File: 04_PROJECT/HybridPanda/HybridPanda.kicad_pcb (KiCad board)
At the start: 4 copper layers, 47.5 x 41.7 mm, 114 parts, among them J1 SWD, P1 TYPE-C-31-M-04, Q1 DDTA143ECA-7-F P08, Q2 DDTA143ECA-7-F P08, Q3 PDTC114EU, Q4 HY12P03C2, SW1 SW_Push, U1 AP22615AWU-7, U10 TJA1042TK-3, U11 TJA1042TK-3, U12 XL1509-3.3, U3 10_0_QHHTZB6_3, U5 FM-B1921RGBA-SH, U6 TPS5450DDAR, U7 STM32H725ZGT6, U8 TJA1042TK-3, U9 TJA1042TK-3, Y1 25MHz X322525MOB4SI

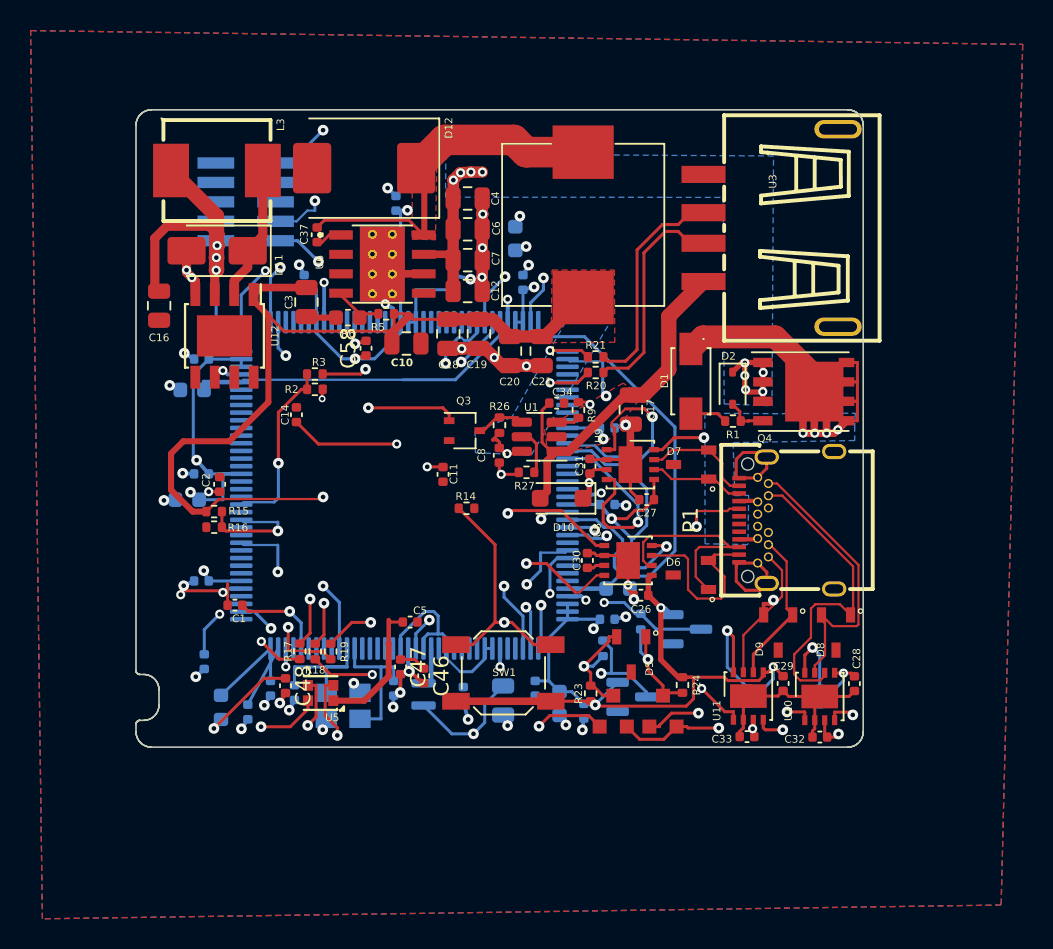
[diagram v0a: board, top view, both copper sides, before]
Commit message: STEP 5: board +5 mm S, U7 +3V3 vias, zone-stub cleanup fix, step5c island/connect_any, D-21..D-24
WIP: pipeline 5a->5b->FR->5c must be rerun from scratch after this commit.

Co-authored-by: Copilot <223556219+Copilot@users.noreply.github.com>
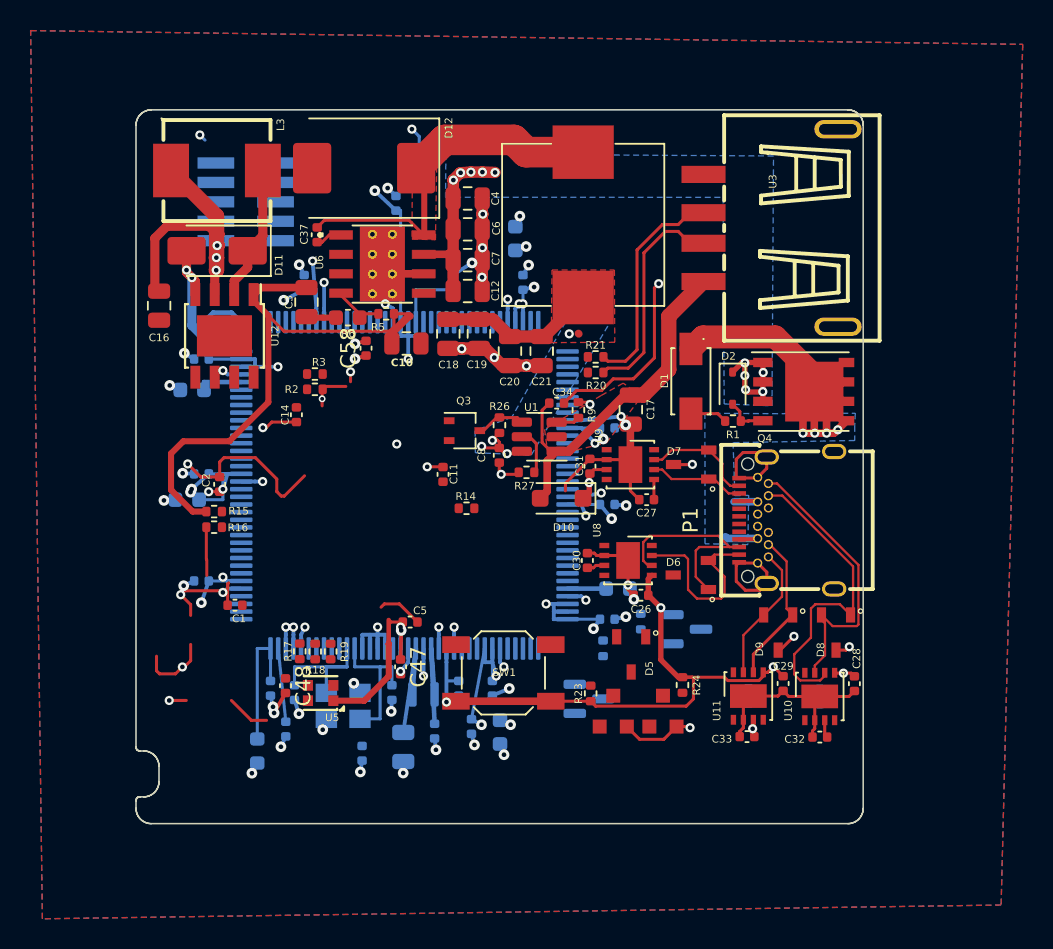
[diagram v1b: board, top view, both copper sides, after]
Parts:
- C46: moved to B.Cu
- moved C38 11.9 mm to (106.7, 74.1)
- moved C63 7.41 mm to (113.9, 72.4)
- moved C42 7.20 mm to (109.4, 73.7)
- moved C60 4.31 mm to (115.8, 72.7)
- moved FB1 3.71 mm to (99.9, 74.0)
- moved C41 3.05 mm to (111.5, 72.7)
- moved D14 2.80 mm to (121.6, 70.6)
- moved C45 2.80 mm to (115.2, 69.9)
- moved C43 2.72 mm to (101.8, 72.5)
- moved C46 2.43 mm to (113.0, 69.9)
- moved C23 0.31 mm to (108.7, 70.1)
- turned L5 to 180 degrees
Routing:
- net GND: track 106.5 -> 181.3 mm, vias 51 -> 66
- net +3V3: track 252.4 -> 187.3 mm, vias 22 -> 40
- net NRST: track 55.1 -> 0.00 mm, vias 3 -> 0
- net VCAP: track 52.0 -> 5.47 mm
- net 12V_Protected: track 61.9 -> 20.1 mm
- net BUS1O_RX: track 38.5 -> 0.00 mm, vias 2 -> 0
- net SBU2_ADC: track 34.4 -> 0.00 mm, vias 2 -> 0
- net BUS1O_TX: track 33.8 -> 0.00 mm, vias 2 -> 0
- net SBU1_ADC: track 33.4 -> 0.00 mm, vias 2 -> 0
- net relay_SBU2: track 33.0 -> 0.00 mm, vias 2 -> 0
- net +5V: track 112.3 -> 82.2 mm, vias 7 -> 8
- net BUS1N_STB: track 29.1 -> 0.00 mm, vias 2 -> 0
- net SBU2: track 27.7 -> 0.00 mm, vias 1 -> 0
- net BUS1N_RX: track 26.2 -> 0.00 mm, vias 2 -> 0
- net LED_BLUE: track 25.5 -> 0.00 mm, vias 2 -> 0
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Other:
- board size 47.5 x 41.7 mm -> 47.5 x 46.7 mm

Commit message: STEP 5-9: PCB routed (DRC 0 unconnected), STEP 6-8 reports, fabrication package (NAO FABRICAR), final report
- STEP 5: pipeline 5a->5b->5c->5d final (run 20), board snapshot .step5_final, DRC 179 (baseline 194), 0 unconnected/clearance/shorts; D-30 extended, D-31 (silk refs)
- STEP 6: step6_reports.py on final board (analytic impedance, skew, vias)
- STEP 7: step7_validate.py - ERC 0 errors, netlist sch x pcb 0 divergences, BOM consistent, parity red_h7 36/36, manifests (ORIGINAL IDENTICAL)
- STEP 8: step8_fabricate.py - gerbers/Excellon/PDF/STEP/BOM_JLC/CPL_JLC + LEIA-ME with blockers
- STEP 9: bring-up plan, RELATORIO_FINAL.md, PROGRESS.md, manifests STEP7/STEP9
- cleanup of tmp probes and pre5c snapshots

Co-authored-by: Copilot <223556219+Copilot@users.noreply.github.com>
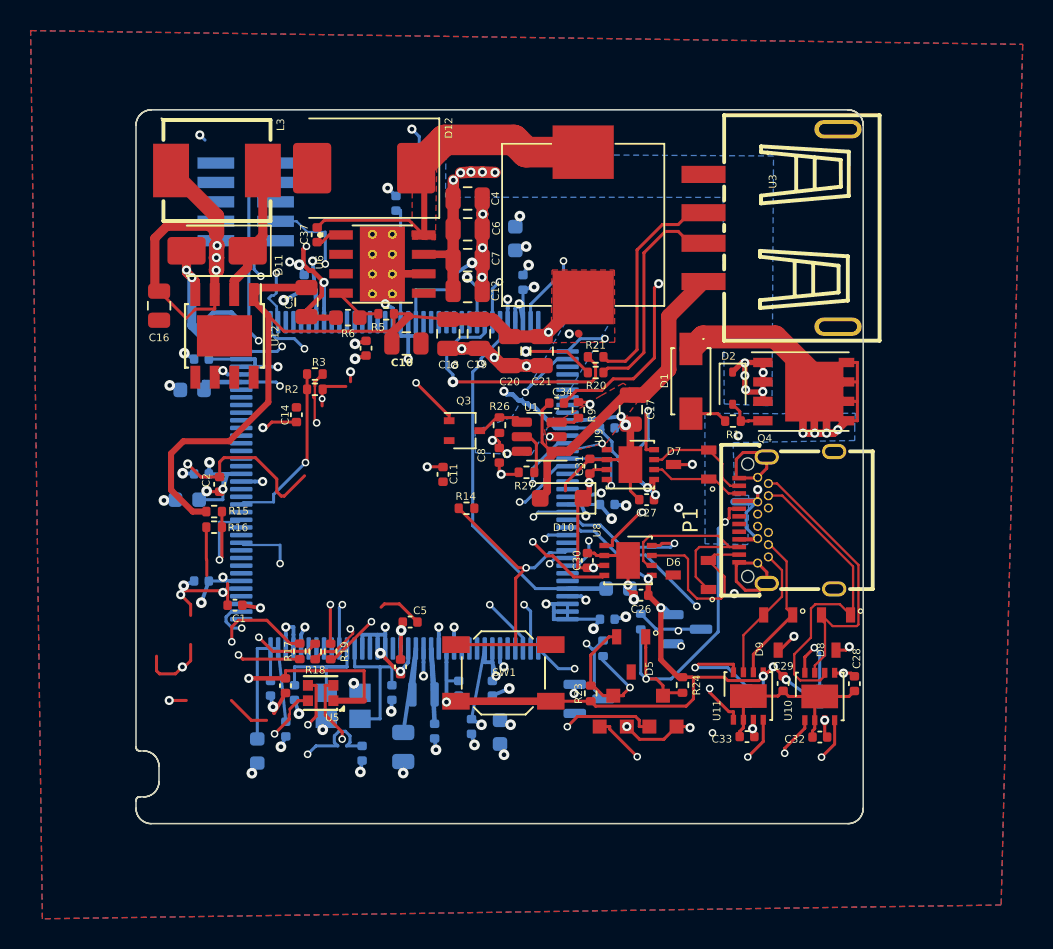
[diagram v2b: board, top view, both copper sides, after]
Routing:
- net +3V3: track 187.3 -> 291.2 mm, vias 40 -> 42
- net NRST: track 0.00 -> 54.0 mm, vias 0 -> 3
- net 12V_Protected: track 20.1 -> 67.4 mm, vias 10 -> 11
- net relay_SBU1: track 0.00 -> 45.4 mm, vias 0 -> 2
- net VCAP: track 5.47 -> 49.0 mm, vias 0 -> 2
- net relay_SBU2: track 0.00 -> 38.9 mm, vias 0 -> 2
- net SBU1_ADC: track 0.00 -> 37.9 mm, vias 0 -> 2
- net BUS1O_TX: track 0.00 -> 37.7 mm, vias 0 -> 2
- net SBU2: track 0.00 -> 32.9 mm, vias 0 -> 1
- net +5V: track 82.2 -> 114.4 mm, vias 8 -> 11
- net BUS1N_TX: track 0.00 -> 30.7 mm, vias 0 -> 3
- net SBU2_ADC: track 0.00 -> 30.6 mm, vias 0 -> 2
- net LED_BLUE: track 0.00 -> 30.3 mm, vias 0 -> 2
- net BUS1O_RX: track 0.00 -> 30.1 mm, vias 0 -> 2
- net BUS0_STB: track 0.00 -> 29.4 mm, vias 0 -> 2
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
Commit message: PCB audit fixes: 42/47 via-in-pad removed, fiducials, D7/D8 moves, +3V3 widening; final_audit/fix_audit/fix_vip_rest scripts and reports (4 via-in-pad pending, DRC not re-run)
Co-authored-by: Copilot <223556219+Copilot@users.noreply.github.com>
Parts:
- added FID1: Fiducial, Fiducial:Fiducial_1mm_Mask2mm, F.Cu at (94.0, 72.3)
- added FID2: Fiducial, Fiducial:Fiducial_1mm_Mask2mm, F.Cu at (137.5, 35.3)
- added FID3: Fiducial, Fiducial:Fiducial_1mm_Mask2mm, F.Cu at (96.8, 35.3)
- added FID4: Fiducial, Fiducial:Fiducial_1mm_Mask2mm, B.Cu at (94.0, 72.3)
- added FID5: Fiducial, Fiducial:Fiducial_1mm_Mask2mm, B.Cu at (137.5, 35.3)
- added FID6: Fiducial, Fiducial:Fiducial_1mm_Mask2mm, B.Cu at (94.0, 43.7)
- moved D7 0.35 mm to (128.5, 55.5)
- moved D8 0.17 mm to (137.5, 66.2)
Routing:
- net GND: track 190.3 -> 225.7 mm
- net +3V3: track 291.2 -> 316.6 mm
- net +5V: track 114.4 -> 119.9 mm
- net +12V: track 44.2 -> 45.3 mm
- net BUS2_TX: track 2.81 -> 3.39 mm

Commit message: PCB: fix DRC regressions from audit pass (via in SW1 keepout, BUS2_H/BUS1N_L clearance to TVS, dangling +5V, FID2/FID5 relocated), U9.4 via-in-pad; step7/step8/final_audit re-run (DRC 0 clearance/0 unconnected, 186 vs baseline 194); fiducials board-only in checks; fab notes list 4 remaining via-in-pad as VIPPO
Co-authored-by: Copilot <223556219+Copilot@users.noreply.github.com>
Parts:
- moved FID2 40.3 mm to (128.4, 74.5)
- moved FID5 40.3 mm to (128.4, 74.5)
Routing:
- net +5V: track 119.9 -> 118.6 mm
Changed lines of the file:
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@@
 	(footprint "Fiducial:Fiducial_1mm_Mask2mm"
 		(layer "F.Cu")
-		(at 137.484998 35.26)
+		(at 128.41 74.51)
 		(property "Reference" "FID2"
 			(at 0 0 0)
@@
 	(footprint "Fiducial:Fiducial_1mm_Mask2mm"
 		(layer "B.Cu")
-		(at 137.484998 35.26 180)
+		(at 128.41 74.51 180)
 		(property "Reference" "FID5"
 			(at 0 0 0)
@@
 	)
 	(via
-		(at 115.25 68.7525)
+		(at 115.3 68.752)
 		(size 0.6)
 		(drill 0.3)
@@
 	(segment
 		(start 115.25 69.3825)
-		(end 115.25 68.7525)
+		(end 115.3 68.752)
 		(width 0.25)
 		(layer "B.Cu")
@@
 	(segment
 		(start 115.25 68.1625)
-		(end 115.25 68.7525)
+		(end 115.3 68.752)
 		(width 0.25)
 		(locked yes)
@@
 	(segment
 		(start 129.64 54.54)
-		(end 130.2795 55.1795)
+		(end 130.36 55.179)
 		(width 0.15)
 		(locked yes)
@@
 	)
 	(segment
-		(start 130.2795 55.1795)
-		(end 130.2795 56.1195)
+		(start 130.36 55.179)
+		(end 130.36 56.12)
 		(width 0.15)
 		(locked yes)
@@
 	)
 	(segment
-		(start 130.2795 56.1195)
+		(start 130.36 56.12)
 		(end 130.790031 56.630031)
 		(width 0.15)
@@
 	)
 	(segment
-		(start 118.918 46.5917)
-		(end 120.1667 46.5917)
-		(width 0.2)
-		(layer "In2.Cu")
-		(net "+5V")
-	)
-	(segment
 		(start 132.82 71.95)
 		(end 132.26 72.51)
@@
 	)
 	(segment
-		(start 123.02 56.62)
-		(end 122.72 56.22)
-		(width 0.15)
-		(locked yes)
+		(start 122.72 56.22)
+		(end 122.959123 56.699335)
+		(width 0.25)
 		(layer "F.Cu")
 		(net "BUS2_RX")
 	)
 	(via
-		(at 123.02 56.62)
+		(at 122.959123 56.699335)
 		(size 0.5)
 		(drill 0.3)
@@
 	(segment
 		(start 123.02 54.85)
-		(end 123.02 56.62)
+		(end 122.959123 56.699335)
 		(width 0.15)
 		(locked yes)
@@
 	(segment
 		(start 136.07 64.655)
-		(end 136.355 64.37)
+		(end 136.07 64.27)
 		(width 0.15)
 		(locked yes)
@@
 	)
 	(segment
-		(start 137.96 64.37)
+		(start 137.96 64.27)
 		(end 138.489998 65.07)
 		(width 0.15)
@@
 	)
 	(segment
-		(start 136.355 64.37)
-		(end 137.96 64.37)
+		(start 136.07 64.27)
+		(end 137.96 64.27)
 		(width 0.15)
 		(locked yes)
@@
 		(polygon
 			(pts
-				(xy 138.684998 35.26) (xy 138.644108 35.570582) (xy 138.524228 35.86) (xy 138.333526 36.108528)
-				(xy 138.084998 36.29923) (xy 137.79558 36.41911) (xy 137.484998 36.46) (xy 137.174415 36.41911)
-				(xy 136.884998 36.29923) (xy 136.636469 36.108528) (xy 136.445767 35.86) (xy 136.325887 35.570582)
-				(xy 136.284998 35.26) (xy 136.325887 34.949417) (xy 136.445767 34.66) (xy 136.636469 34.411471)
-				(xy 136.884998 34.220769) (xy 137.174415 34.100889) (xy 137.484998 34.06) (xy 137.79558 34.100889)
-				(xy 138.084998 34.220769) (xy 138.333526 34.411471) (xy 138.524228 34.66) (xy 138.644108 34.949417)
+				(xy 127.31 73.41) (xy 129.51 73.41) (xy 129.51 75.61) (xy 127.31 75.61)
 			)
 		)
@@
 		(polygon
 			(pts
-				(xy 138.684998 35.26) (xy 138.644108 35.570582) (xy 138.524228 35.86) (xy 138.333526 36.108528)
-				(xy 138.084998 36.29923) (xy 137.79558 36.41911) (xy 137.484998 36.46) (xy 137.174415 36.41911)
-				(xy 136.884998 36.29923) (xy 136.636469 36.108528) (xy 136.445767 35.86) (xy 136.325887 35.570582)
-				(xy 136.284998 35.26) (xy 136.325887 34.949417) (xy 136.445767 34.66) (xy 136.636469 34.411471)
-				(xy 136.884998 34.220769) (xy 137.174415 34.100889) (xy 137.484998 34.06) (xy 137.79558 34.100889)
-				(xy 138.084998 34.220769) (xy 138.333526 34.411471) (xy 138.524228 34.66) (xy 138.644108 34.949417)
+				(xy 127.31 73.41) (xy 129.51 73.41) (xy 129.51 75.61) (xy 127.31 75.61)
 			)
 		)

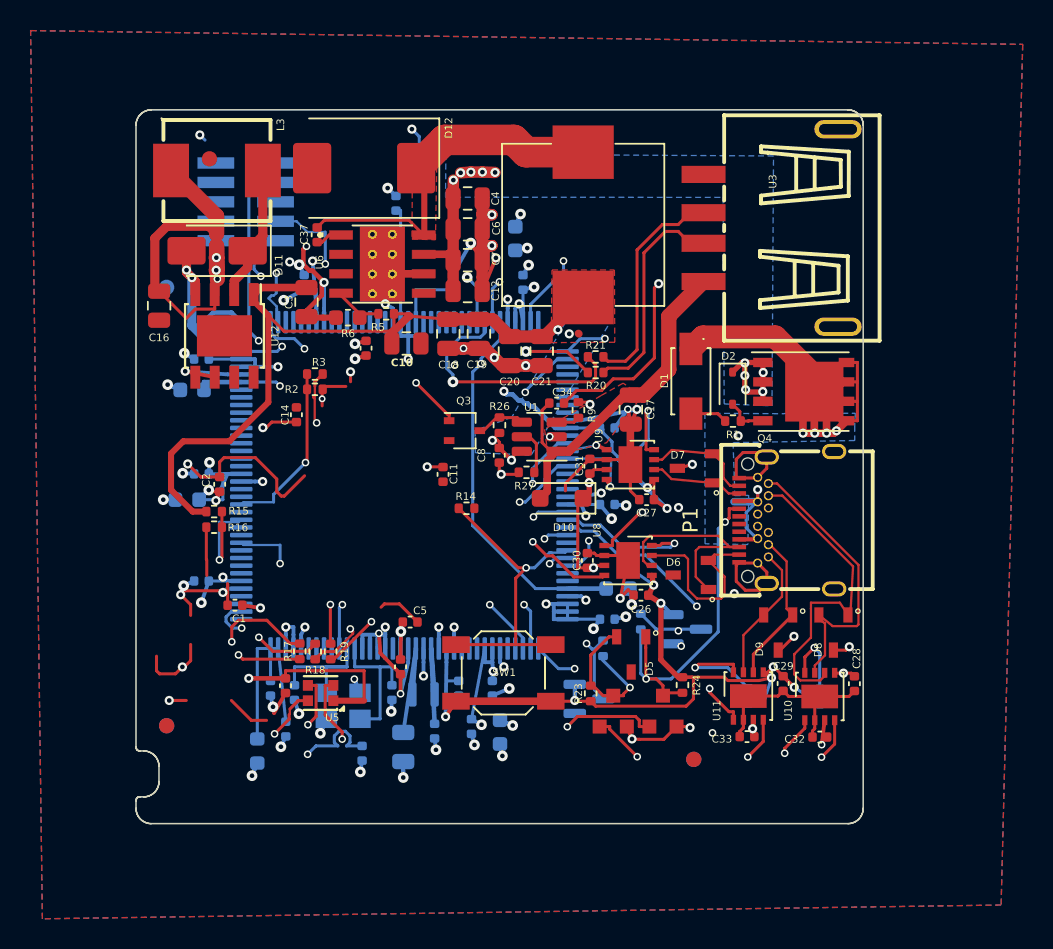
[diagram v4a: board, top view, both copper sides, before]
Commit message: PCB relayout east +3 mm: eliminate remaining via-in-pad, DRC 0/0
Widen the Hybrid Panda board 3 mm to the east (x_max 139.535 -> 142.535,
board 50.625 x 46.75 mm) and spread the transceiver/protection cluster
(U8-U11, D5-D9, D13, P1, U3, Q1/Q2, R24, C26-C33) so the last four
via-in-pad (D13.1, U1.2, C30.2, C33.2) have room; full reroute.

- 05_SCRIPTS/step5e_relayout_east.py: new step between 5a and 5b; moves
  Edge.Cuts, zones, drawings and the east block; report step5e_relayout_east.json
- step5b_route.py: phase M routes the U1.2 GND via outside the pad via a
  USB_PWR detour; +3V3 In1 zone outline to x = 130
- fix_audit.py: D7 x U9 courtyard solved by moving U9 west first
- fix_drc_relayout.py: DRC-uuid-driven fixer replacing the coordinate-bound
  fix_drc_regressions.py (SW1 keepout via, via x via hole clearance,
  dangling track, FID2/FID5 relocation)
- fix_vip_reroute.py: last-resort via-in-pad mover (U8.3 +5V via moved to
  the F.Cu track west of C30, B.Cu track rerouted)
- step8_fabricate.py: via-in-pad note updated

Results (kicad-cli DRC): 0 clearance / 0 unconnected / 182 total;
final_audit via-in-pad 0, shorts 0; step7_validate failures empty
(ERC 0 errors, netlist 0 divergences, parity 0 conflicts). Reports in
06_REPORTS, fabrication outputs regenerated in 07_FABRICATION. Docs:
README (STEP 5e), DECISIONS D-32/D-33, PROGRESS, RELATORIO_FINAL.

Co-authored-by: Copilot <223556219+Copilot@users.noreply.github.com>
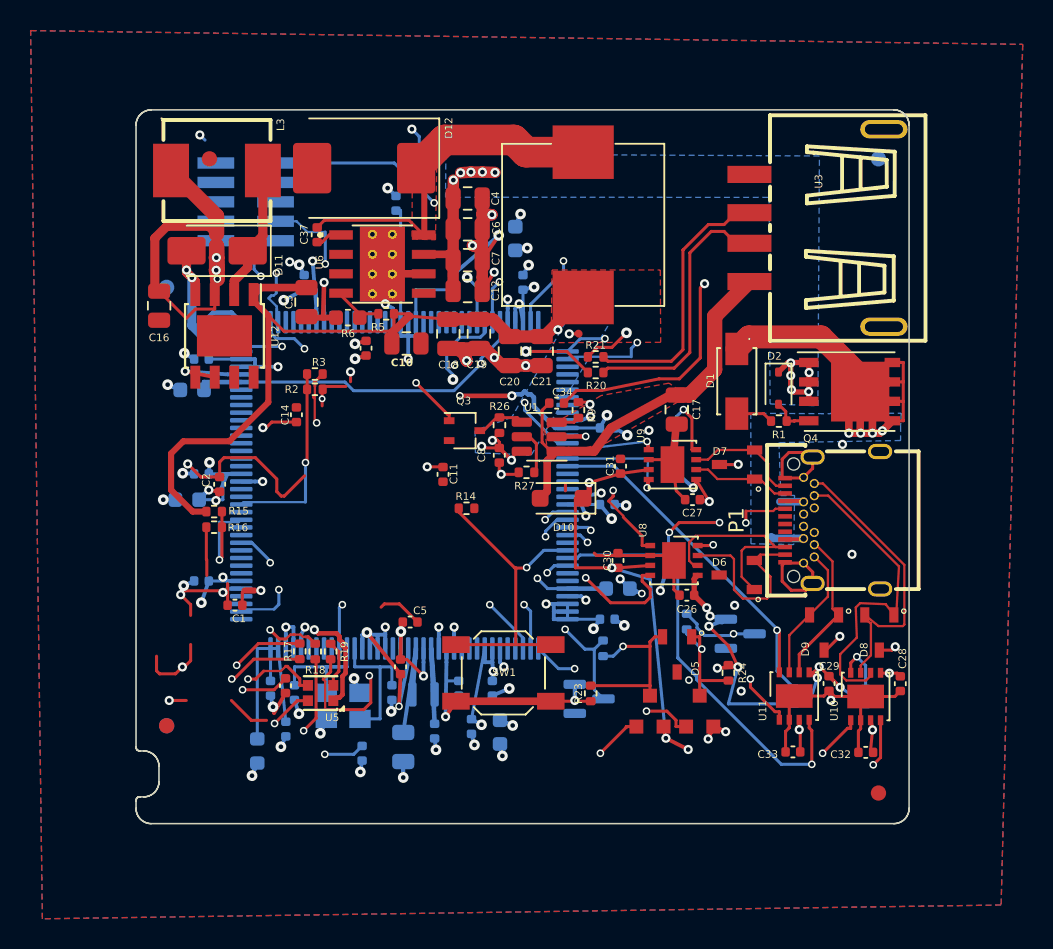
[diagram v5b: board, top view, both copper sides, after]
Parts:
- moved FID5 41.1 mm to (140.5, 35.3)
- moved FID2 12.3 mm to (140.5, 76.7)
- moved D13 3.51 mm to (131.4, 66.3)
- moved C32 3.16 mm to (139.7, 74.1)
- moved C33 3.16 mm to (134.9, 74.0)
- moved R24 3.10 mm to (130.7, 68.8)
- moved C27 3.00 mm to (128.3, 57.5)
- moved C17 3.00 mm to (127.3, 51.6)
- moved C26 3.00 mm to (128.0, 63.8)
- moved C28 3.00 mm to (141.9, 69.6)
- moved C29 3.00 mm to (137.3, 69.6)
- moved D1 3.00 mm to (131.2, 49.8)
- moved D2 3.00 mm to (133.9, 50.2)
- moved D5 3.00 mm to (127.3, 67.7)
- moved D6 3.00 mm to (131.2, 62.5)
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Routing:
- net RED-: track 18.8 -> 3.10 mm, vias 2 -> 0
- net +5V: track 118.6 -> 130.7 mm, vias 11 -> 14
- net BUS1O_STB: track 9.39 -> 21.1 mm, vias 1 -> 4
- net GREEN-: track 23.6 -> 12.4 mm
- net relay_SBU1: track 45.4 -> 35.1 mm
- net LED_GREEN: track 19.0 -> 28.3 mm
- net LED_RED: track 15.6 -> 22.1 mm
- net BUS1O_RX: track 30.1 -> 36.1 mm
- net BUS0_RX: track 22.8 -> 28.6 mm, vias 2 -> 1
- net VCAP: track 49.0 -> 43.6 mm
- net BUS1O_TX: track 37.7 -> 32.5 mm
- net SBU1_ADC: track 37.9 -> 42.6 mm, vias 2 -> 3
- net USB_D+: track 16.9 -> 21.5 mm, vias 1 -> 2
- net BUS1N_TX: track 30.7 -> 35.3 mm, vias 3 -> 2
- net BUS0_STB: track 29.4 -> 25.3 mm, vias 2 -> 1
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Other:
- board size 47.5 x 46.7 mm -> 50.5 x 46.7 mm

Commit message: pcb: step 1 - apply footprint audit fixes (Q1/Q2/Q3 pads, U5, U12 EP, P1 ring, R6 R_0603, SMD attrs, 3D)
- Q3 SOT-323 pads to KiCad geometry; Q1/Q2 SOT-23 pads 0.6x1.475 + courtyard 3.1x3.5
- U5 LED pads y +/-0.60 per FM-B1921RGBA-SH datasheet
- U12 XL1509: EP pads lose paste/mask (SOP-8 without EP), SOIC-8 3D model
- P1 TYPE-C: THT pads B1-B12 0.60 -> 0.65, 12 stray F.Paste circles removed
- footprint attribute THT -> SMD on D1, D5-D9, Q1, Q2, U5, L3; L3 courtyard 8.9x6.8
- 3D models for D8/D9 (SOT-23) and Q4 (PowerPAK SO-8 step)
- R6 footprint Capacitor_SMD:C_0603 -> Resistor_SMD:R_0603 (schematic + board, nets kept)
- local reroute: relay_SBU1 via moved out of Q1 pad 3, R24 -0.35 mm, LED_RED nudged
- DRC 0 clearance / 0 unconnected / 181 (182 -> 181: -10 footprint_type, +10 lib mismatch, -1 text)
- new helpers 05_SCRIPTS/corr_gate.py, corr_step1_footprints.py, corr_step1b_fix.py, tools/dump_geom.py

Co-authored-by: Copilot <223556219+Copilot@users.noreply.github.com>
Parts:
- R6: footprint Capacitor_SMD:C_0603_1608Metric -> Resistor_SMD:R_0603_1608Metric
- moved R24 0.35 mm to (130.7, 68.5)
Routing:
- net relay_SBU1: track 35.1 -> 33.0 mm
